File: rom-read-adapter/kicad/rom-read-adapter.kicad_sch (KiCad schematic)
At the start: 66 parts, among them J1 ZIF-48, J2 Conn_01x04_Pin

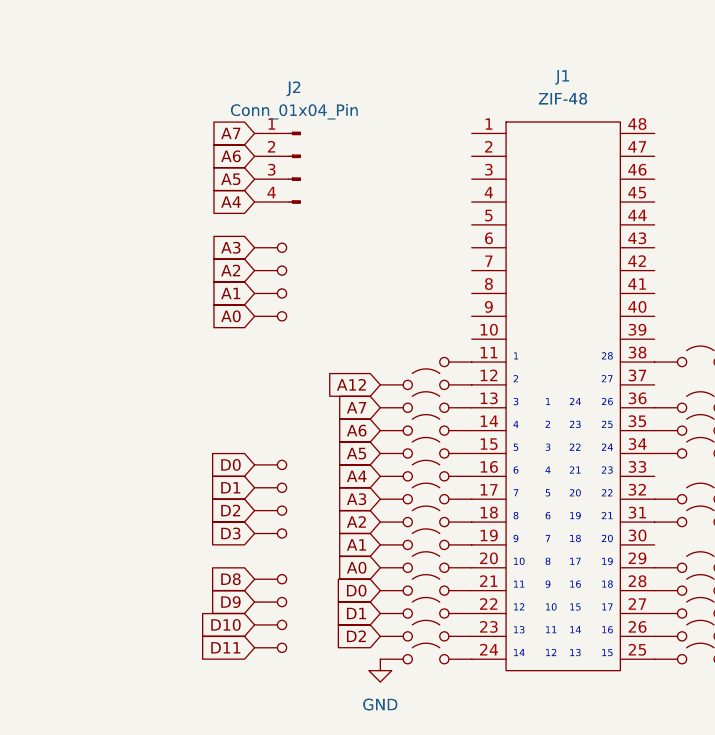
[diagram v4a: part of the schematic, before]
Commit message: WIP rom-read-adapter sch: Start using pin headers
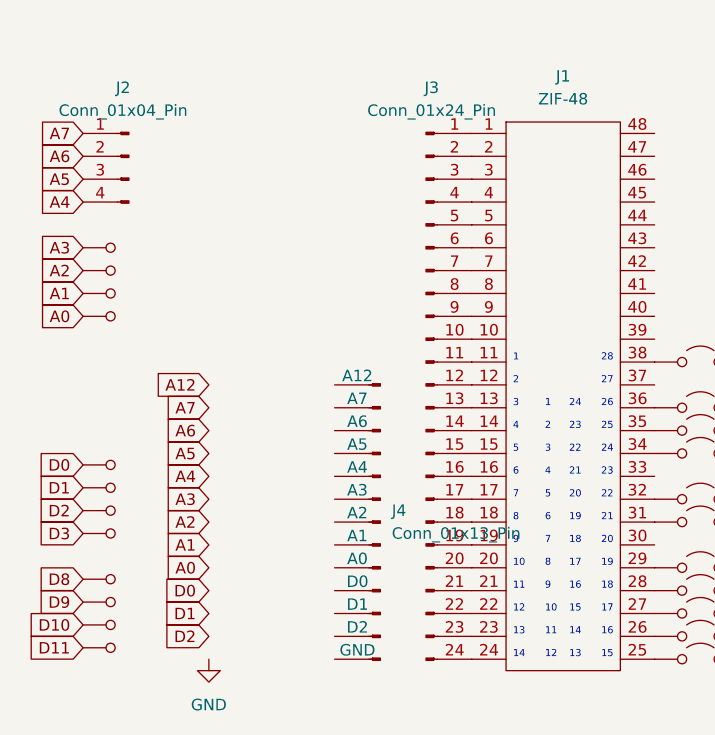
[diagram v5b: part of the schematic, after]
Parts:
- removed JP11: Header_Pin, symbol 0cjs-hwdev:Header_Pin
- removed JP12, JP13, JP14, JP15, JP16, JP17, JP18, JP19, JP20, JP21, JP22, JP23, JP24: Jumper_2_Open, symbol Jumper:Jumper_2_Open
- added J3: Conn_01x24_Pin, symbol Connector:Conn_01x24_Pin
- added J4: Conn_01x13_Pin, symbol Connector:Conn_01x13_Pin
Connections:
- net at J1.1: now also J3.1 (Pin_1)
- net at J1.10: now also J3.10 (Pin_10)
- net at J1.11: now also J3.11 (Pin_11)
- net at J1.12: now also J3.12 (Pin_12)
- net at J1.13: now also J3.13 (Pin_13)
- net at J1.14: now also J3.14 (Pin_14)
- net at J1.15: now also J3.15 (Pin_15)
- net at J1.16: now also J3.16 (Pin_16)
- net at J1.17: now also J3.17 (Pin_17)
- net at J1.18: now also J3.18 (Pin_18)
- net at J1.19: now also J3.19 (Pin_19)
- net at J1.2: now also J3.2 (Pin_2)
- net at J1.20: now also J3.20 (Pin_20)
- net at J1.21: now also J3.21 (Pin_21)
- net at J1.22: now also J3.22 (Pin_22)
- net at J1.23: now also J3.23 (Pin_23)
- net at J1.24: now also J3.24 (Pin_24)
- net at J1.3: now also J3.3 (Pin_3)
- net at J1.4: now also J3.4 (Pin_4)
- net at J1.5: now also J3.5 (Pin_5)
- net at J1.6: now also J3.6 (Pin_6)
- net at J1.7: now also J3.7 (Pin_7)
- net at J1.8: now also J3.8 (Pin_8)
- net at J1.9: now also J3.9 (Pin_9)
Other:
- moved on the sheet: J2

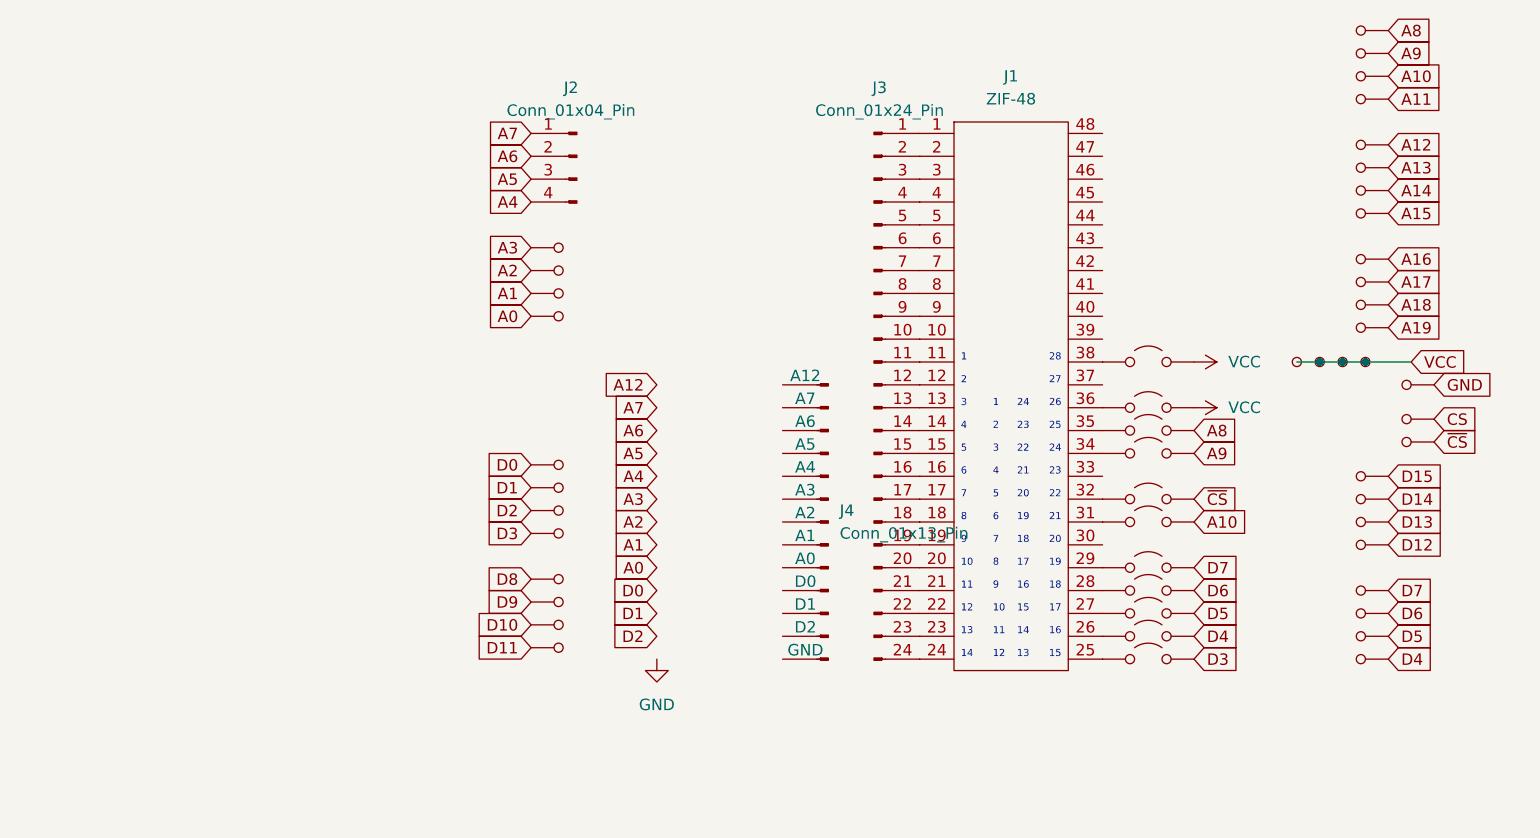
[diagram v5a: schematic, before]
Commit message: WIP rom-read-adapter sch: Add 50 pin connector to SuperAKI
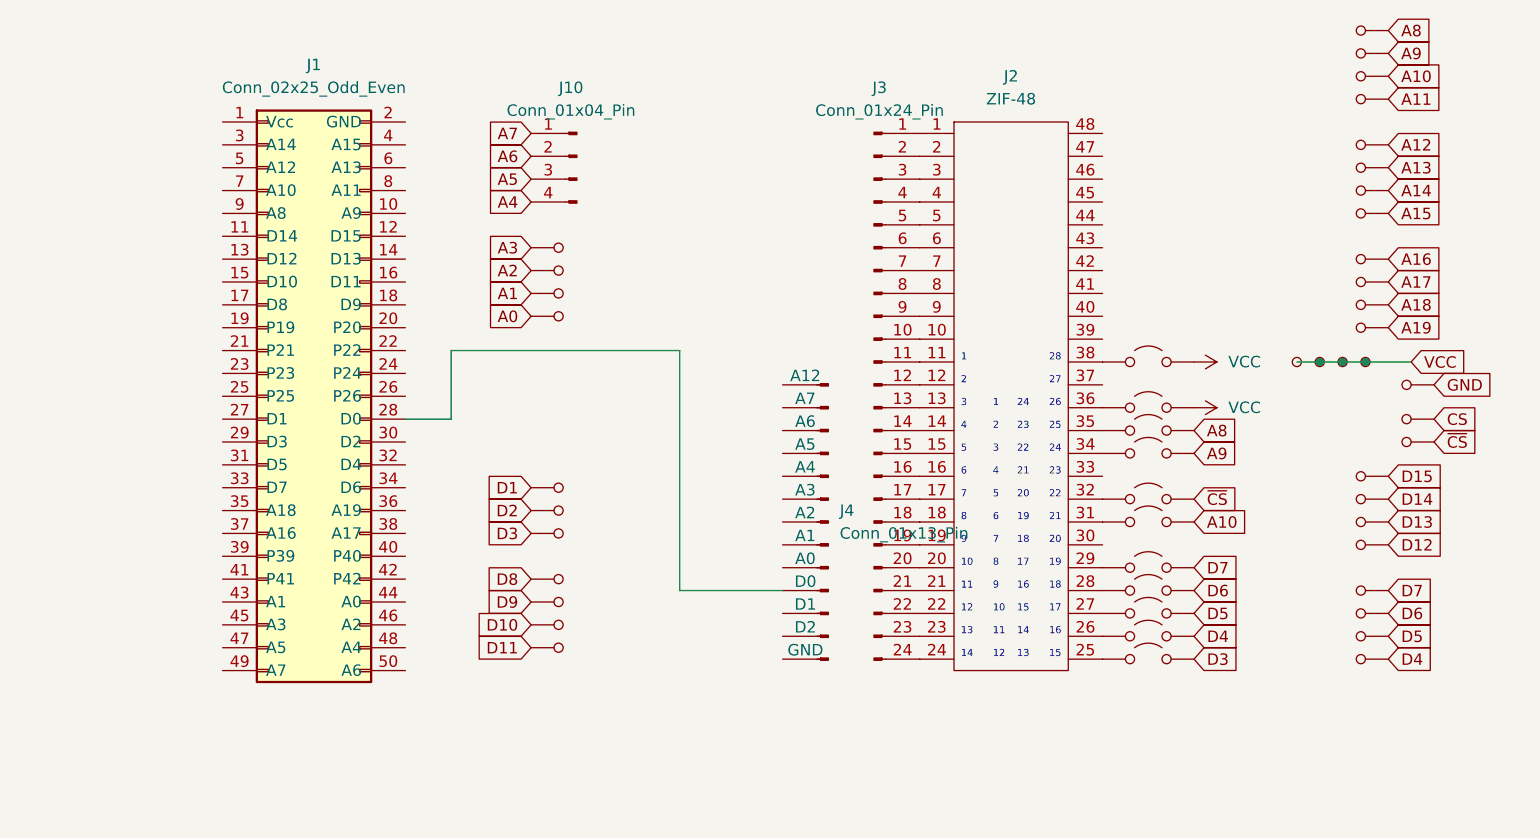
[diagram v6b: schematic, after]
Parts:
- removed JPA33: Header_Pin, symbol 0cjs-hwdev:Header_Pin
- added J1: Conn_02x25_Odd_Even, symbol Connector_Generic:Conn_02x25_Odd_Even
- renumbered J2 to J10, J1 to J2
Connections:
- net at J4.10 (D0): now also J1.28 (D0)

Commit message: WIP rom-read-adapter sch: Finish nets for J1 J4 connections
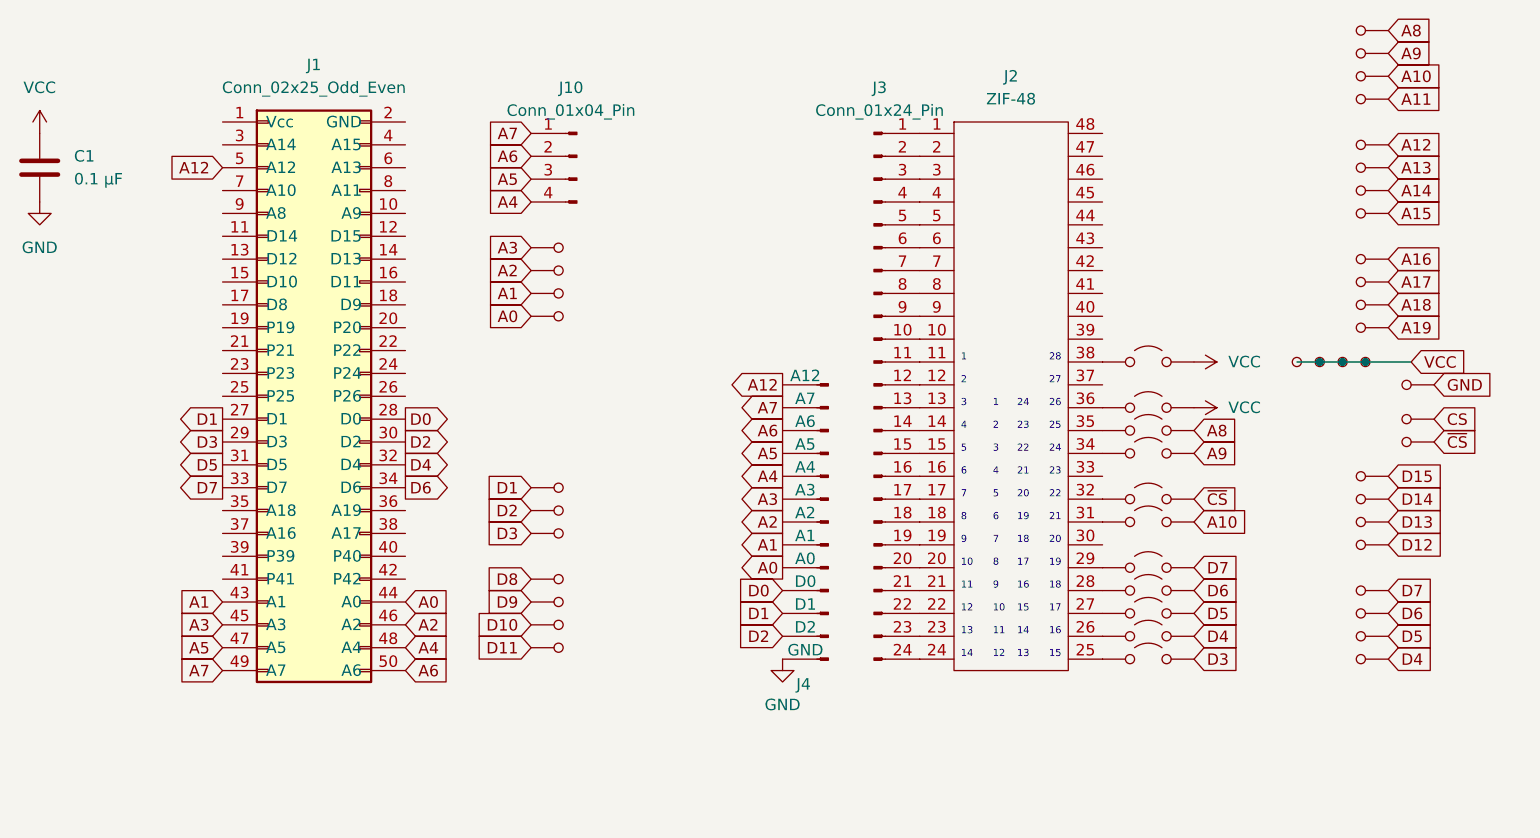
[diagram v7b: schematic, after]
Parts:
- added C1: 0.1 μF, symbol Device:C
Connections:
- net A0: now also J1.44 (A0), J4.9 (A0)
- net A1: now also J1.43 (A1), J4.8 (A1)
- net A12: now also J1.5 (A12), J4.1 (A12)
- net A2: now also J1.46 (A2), J4.7 (A2)
- net A3: now also J1.45 (A3), J4.6 (A3)
- net A4: now also J1.48 (A4), J4.5 (A4)
- net A5: now also J1.47 (A5), J4.4 (A5)
- net A6: now also J1.50 (A6), J4.3 (A6)
- net A7: now also J1.49 (A7), J4.2 (A7)
- net D1: now also J1.27 (D1), J4.11 (D1)
- net D2: now also J1.30 (D2), J4.12 (D2)
- net D3: now also J1.29 (D3)
- net D4: now also J1.32 (D4)
- net D5: now also J1.31 (D5)
- net D6: now also J1.34 (D6)
- net D7: now also J1.33 (D7)
- net GND: now also J4.13 (GND), C1.2
- net VCC: now also C1.1
- net D0: now reaches J1.28 (D0), J4.10 (D0)

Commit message: WIP rom-read-adapter sch: Added J5 and moved references.
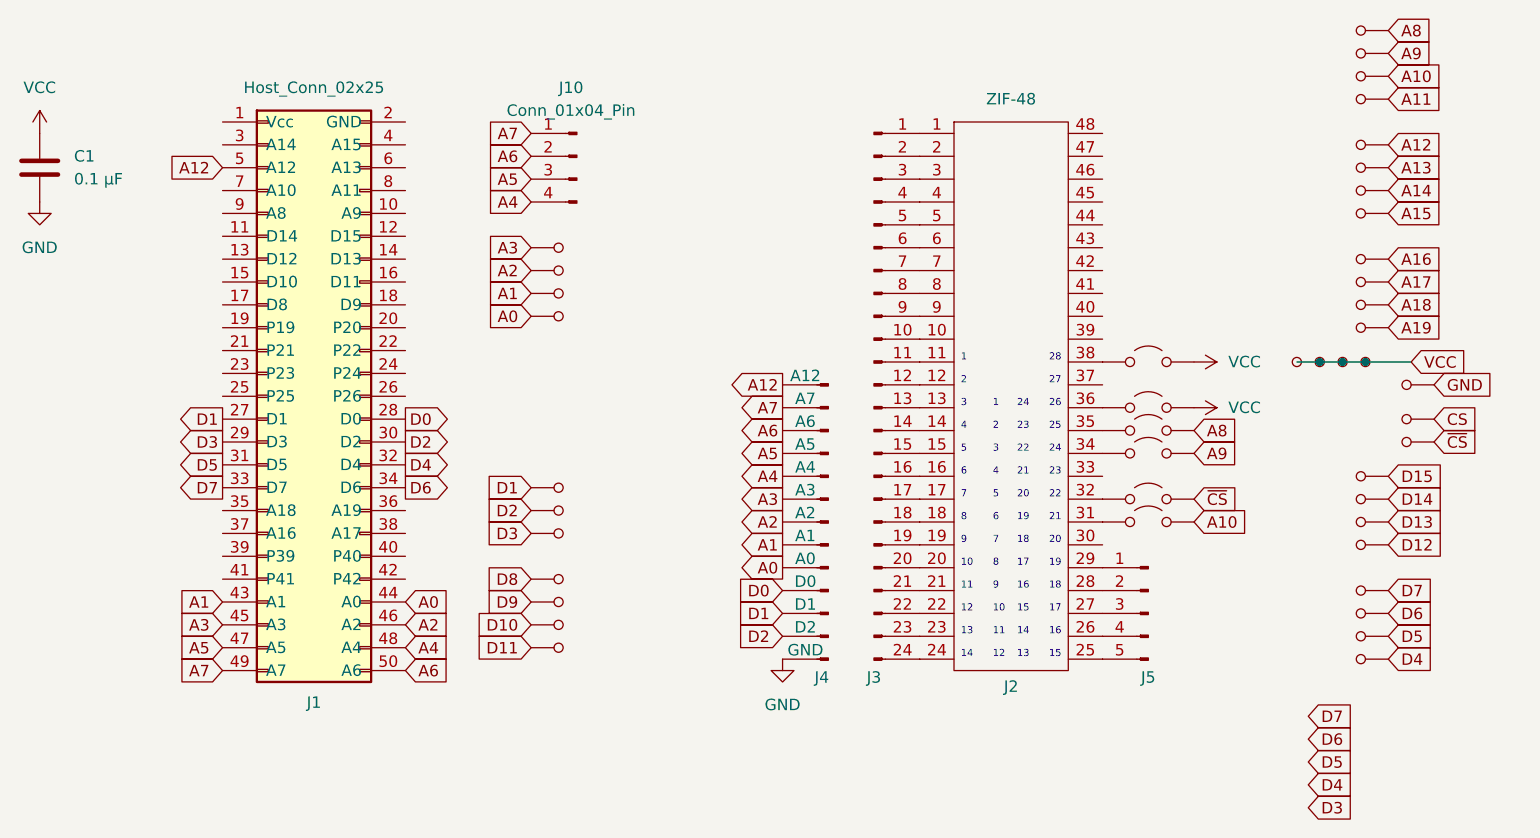
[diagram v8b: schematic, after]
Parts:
- removed JP25, JP26, JP27, JP28, JP29: Jumper_2_Open, symbol Jumper:Jumper_2_Open
- added J5: Conn_01x05_Pin, symbol Connector:Conn_01x05_Pin
- J1: value Conn_02x25_Odd_Even -> Host_Conn_02x25
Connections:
- net at J2., J2.28: now also J5.2 (Pin_2)
- net at J2.25: now also J5.5 (Pin_5)
- net at J2.26: now also J5.4 (Pin_4)
- net at J2.27: now also J5.3 (Pin_3)
- net at J2.29: now also J5.1 (Pin_1)
